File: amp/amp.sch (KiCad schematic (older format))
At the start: 29 parts

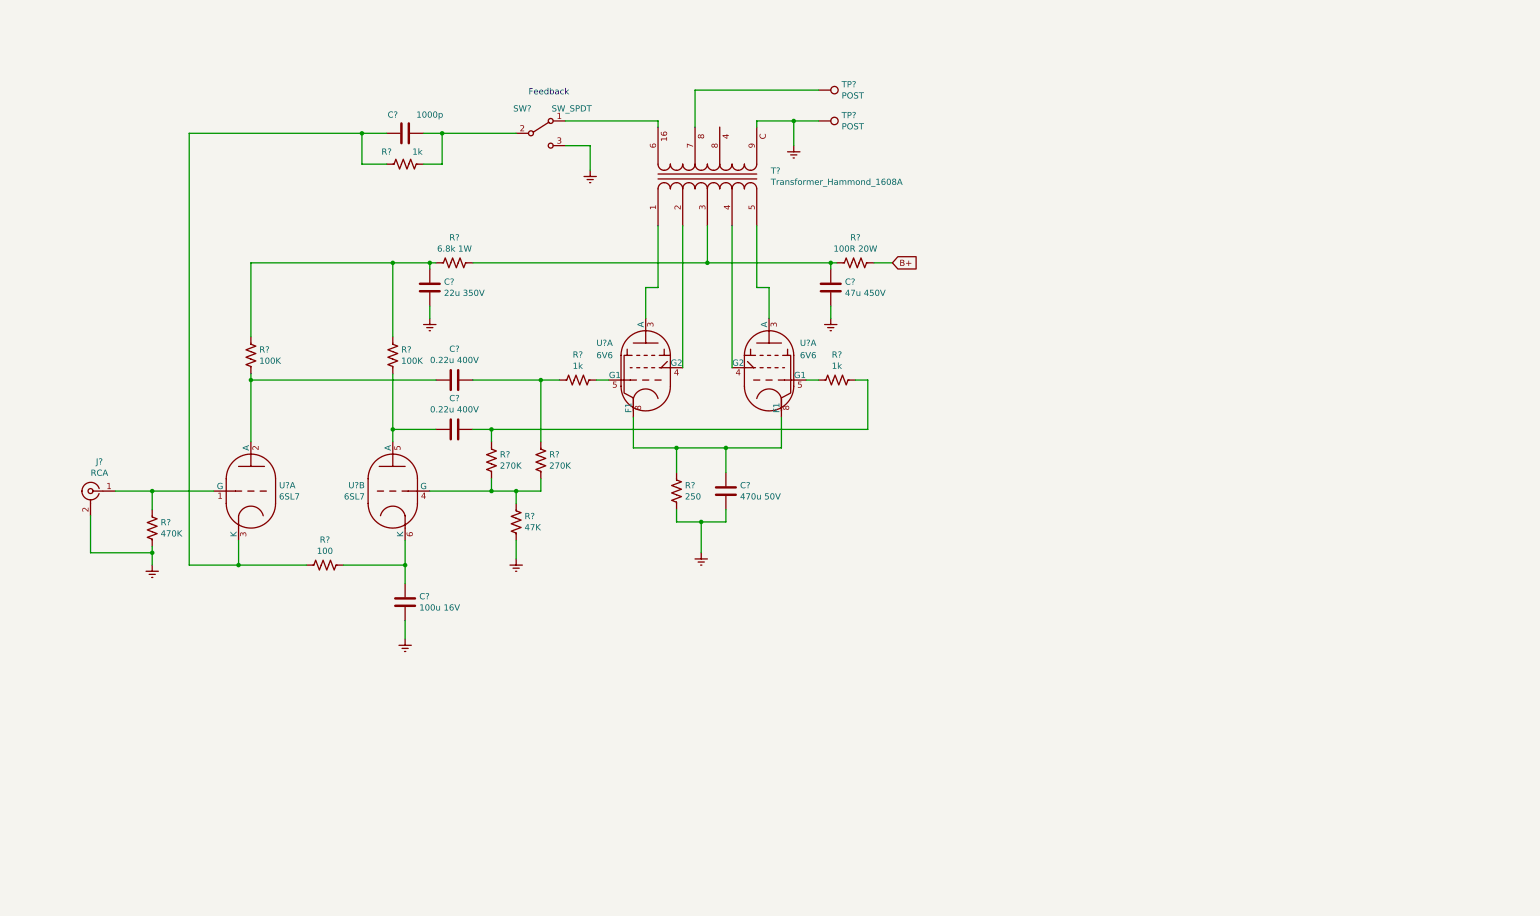
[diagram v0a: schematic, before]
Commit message: draft stereo schem complete
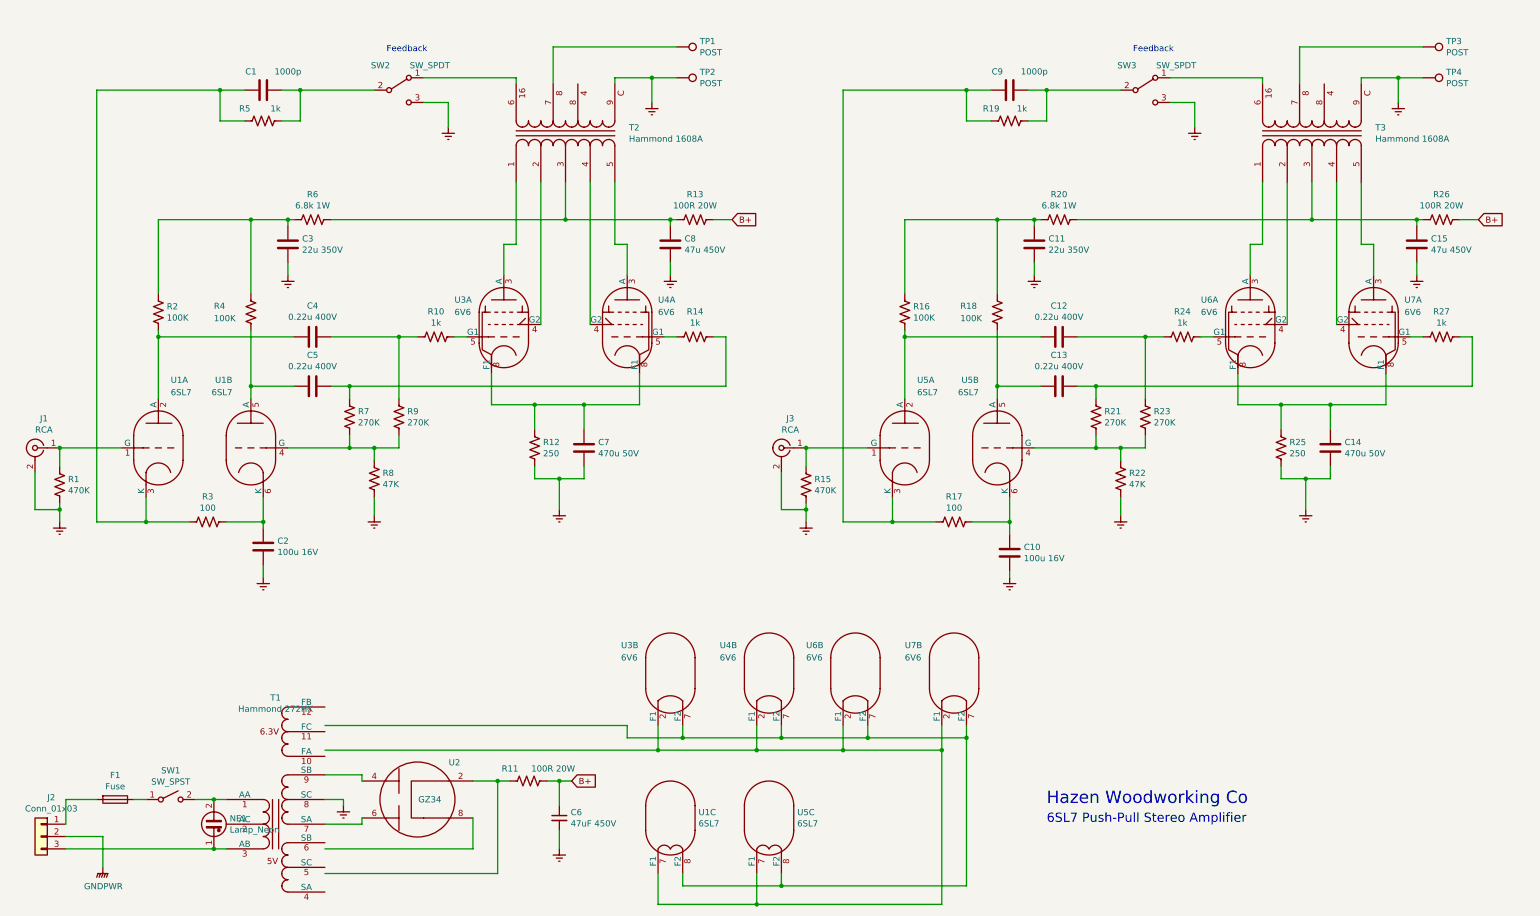
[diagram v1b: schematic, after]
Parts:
- added C10: 100u 16V, symbol Device:C
- added C11: 22u 350V, symbol Device:C
- added C12, C13: 0.22u 400V, symbol Device:C
- added C14: 470u 50V, symbol Device:C
- added C15: 47u 450V, symbol Device:C
- added C6: 47uF 450V, symbol Device:C_Small
- added C9: 1000p, symbol Device:C
- added F1: Fuse, symbol Device:Fuse
- added J2: Conn_01x03, symbol Connector_Generic:Conn_01x03
- added J3: RCA, symbol Connector:Conn_Coaxial
- added NE1: Lamp_Neon, symbol Device:Lamp_Neon
- added R11, R26: 100R 20W, symbol Device:R_US
- added R15: 470K, symbol Device:R_US
- added R16, R18: 100K, symbol Device:R_US
- added R17: 100, symbol Device:R_US
- added R19, R24, R27: 1k, symbol Device:R_US
- added R20: 6.8k 1W, symbol Device:R_US
- added R21, R23: 270K, symbol Device:R_US
- added R22: 47K, symbol Device:R_US
- added R25: 250, symbol Device:R_US
- added SW1: SW_SPST, symbol Switch:SW_SPST
- added SW3: SW_SPDT, symbol Switch:SW_SPDT
- added T1: Hammond 272HX, symbol my_tubes:Transformer_tube_power_dualfil
- added T3: Hammond 1608A, symbol my_tubes:Transformer_Hammond_1608A
- added TP3, TP4: POST, symbol Connector:TestPoint
- added unit 3 of U1
- added U2: GZ34, symbol my_tubes:GZ34
- added unit 2 of U3
- added unit 2 of U4
- added U5: 6SL7, Valve:Valve_Noval_P, symbol my_tubes:6SL7
- added U6, U7: 6V6, Valve:Valve_Octal, symbol my_tubes:6V6
- T2: renamed from T?; value Transformer_Hammond_1608A -> Hammond 1608A
- gave numbers to parts that had none: 27
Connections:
- net B+: now also C6.1, R11.1, R26.1
- net Earth: now also C10.1, C11.1, C14.1, C15.1, C6.2, J3.2 (Ext), R15.2, R22.2, R25.2, SW3.3 (C), T1.8 (SC), T3.9 (BLK), TP4.1
- new net: NE1.2, SW1.2 (B), T1.1 (AA)
- new net: J2.3 (Pin_3), NE1.1, T1.3 (AB)
- new net: T1.7 (SA), U2.6 (A2)
- new net: T1.9 (SB), U2.4 (A1)
- new net: R11.2, U2.2 (K)
- new net: U1.7 (F1), U3.2 (F1), U4.2 (F1), U5.7 (F1), U6.2 (F1), U7.2 (F1)
- new net: U1.8 (F2), U3.7 (F2), U4.7 (F2), U5.8 (F2), U6.7 (F2), U7.7 (F2)
- new net: T3.1 (BLU), U6.3 (A)
- new net: T3.2 (BLU/YEL), U6.4 (G2)
- new net: R24.1, U6.5 (G1)
- new net: C14.2, R25.1, U6.8 (F1), U7.8 (F1)
- new net: J3.1 (In), R15.1, U5.1 (G)
- new net: C12.2, R16.2, U5.2 (A)
- new net: C9.2, R17.2, R19.2, U5.3 (K)
- new net: R21.2, R22.1, R23.2, U5.4 (G)
- new net: C13.2, R18.2, U5.5 (A)
- new net: C10.2, R17.1, U5.6 (K)
- new net: C11.2, R16.1, R18.1, R20.2
- new net: T3.5 (BRN), U7.3 (A)
- new net: T3.4 (BRN/YEL), U7.4 (G2)
- new net: R27.2, U7.5 (G1)
- new net: C12.1, R23.1, R24.2
- new net: C13.1, R21.1, R27.1
- new net: C15.2, R20.1, R26.2, T3.3 (RED)
- new net: SW3.1 (A), T3.6 (WHT)
- new net: T3.7 (YEL), TP3.1
- new net: C9.1, R19.1, SW3.2 (B)
- new net: F1.1, SW1.1 (A)
- new net: F1.2, J2.1 (Pin_1)
- new net GNDPWR: J2.2 (Pin_2)
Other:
- note added: "6SL7 Push-Pull Stereo Amplifier"
- note added: "Hazen Woodworking Co"
- moved on the sheet: C1, C2, C3, C4, C5, C7, C8, J1, R1, R10, R12, R13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

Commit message: starting footprints
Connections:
- net Earth: now also T1.11 (FC)
- net at T1.10 (FA): now also U1.7 (F1), U3.2 (F1), U4.2 (F1), U5.7 (F1), U6.2 (F1), U7.2 (F1)
- net at T1.12 (FB): now also U1.8 (F2), U3.7 (F2), U4.7 (F2), U5.8 (F2), U6.7 (F2), U7.7 (F2)
- net at T1.4 (SA): now also R11.2, U2.2 (K)
- net at T1.6 (SB): now also U2.8 (F2)
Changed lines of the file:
@@
 U 1 1 629E47F8
 P 2650 6900
-F 0 "T1" H 2650 7725 50  0000 C CNN
-F 1 "Hammond 272HX" H 2650 7634 50  0000 C CNN
+F 0 "T1" H 2500 7900 50  0000 C CNN
+F 1 "Hammond 272HX" H 2800 7800 50  0000 C CNN
 F 2 "" H 2650 6700 50  0001 C CNN
 F 3 "~" H 2650 6700 50  0001 C CNN
@@
 	3200 6900 3050 6900
 Wire Wire Line
-	3050 7300 4250 7300
-Wire Wire Line
-	4250 7300 4250 7050
-Wire Wire Line
-	3050 7500 4450 7500
-Wire Wire Line
-	4450 7500 4450 6750
+	3050 7250 4250 7250
+Wire Wire Line
+	4250 7250 4250 7050
+Wire Wire Line
+	3050 7650 4450 7650
+Wire Wire Line
+	4450 7650 4450 6750
 Wire Wire Line
 	4450 6750 4250 6750
@@
 Connection ~ 8250 6400
 Wire Wire Line
-	5750 6500 3050 6500
-Connection ~ 5750 6500
-Wire Wire Line
-	3050 6300 5500 6300
-Wire Wire Line
-	5500 6300 5500 6400
+	3050 6150 5500 6150
+Wire Wire Line
+	5500 6150 5500 6400
 Wire Wire Line
 	5500 6400 5950 6400
@@
 U 1 1 62BAE772
 P 2150 7100
-F 0 "NE1" H 2278 7146 50  0000 L CNN
-F 1 "Lamp_Neon" H 2278 7055 50  0000 L CNN
+F 0 "NE1" H 1850 7100 50  0000 L CNN
+F 1 "Lamp_Neon" H 1850 6800 50  0000 L CNN
 F 2 "" V 2150 7200 50  0001 C CNN
 F 3 "~" V 2150 7200 50  0001 C CNN
@@
 Text Notes 8900 6950 0    100  ~ 0
 Hazen Woodworking Co
+Wire Wire Line
+	3050 6550 5500 6550
+Wire Wire Line
+	5500 6550 5500 6500
+Wire Wire Line
+	5500 6500 5750 6500
+Connection ~ 5750 6500
+$Comp
+L power:Earth #PWR?
+U 1 1 62A64B63
+P 3200 6350
+F 0 "#PWR?" H 3200 6100 50  0001 C CNN
+F 1 "Earth" H 3200 6200 50  0001 C CNN
+F 2 "" H 3200 6350 50  0001 C CNN
+F 3 "~" H 3200 6350 50  0001 C CNN
+	1    3200 6350
+	1    0    0    -1
+$EndComp
+Wire Wire Line
+	3200 6350 3050 6350
 $EndSCHEMATC

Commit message: working on schem
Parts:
- removed J2: Conn_01x03, symbol Connector_Generic:Conn_01x03
- removed T1: Hammond 272HX, symbol my_tubes:Transformer_tube_power_dualfil
- added J?: Conn_01x05, symbol Connector_Generic:Conn_01x05
- added JP?: JPR3, symbol Device:Jumper_NC_Dual
- added R?: RRRRR, symbol Device:R_US
- added T?: Transformer_Hammond_272HX, symbol my_tubes:Transformer_Hammond_272HX
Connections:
- net Earth: now also T?.11 (FC), T?.8 (SC)
- net GNDPWR: now also J?.2 (Pin_2), J?.4 (Pin_4), J?.5 (Pin_5)
- net at SW1.2 (B): now also JP?.2, R?.2; no longer NE1.2
- net at U1.7 (F1), U3.2 (F1), U4.2 (F1)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: now also T?.10 (FA)
- net at U1.8 (F2), U3.7 (F2), U4.7 (F2)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: now also T?.12 (FB)
- net at NE1.1: now also J?.3 (Pin_3), T?.3 (AB)
- net at R11.2, U2.2 (K): now also T?.4 (SA)
- net at U2.8 (F2): now also T?.6 (SB)
- net at U2.6 (A2): now also T?.7 (SA)
- net at U2.4 (A1): now also T?.9 (SB)
- net at F1.2: now also J?.1 (Pin_1)
- new net: JP?.1, T?.1 (AA)
- new net: JP?.3, T?.2 (AC)
- new net: NE1.2, R?.1
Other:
- note added: "117V"
- note added: "125V"
- moved on the sheet: F1, NE1, SW1
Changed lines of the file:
@@
 Feedback
-$Comp
-L my_tubes:Transformer_tube_power_dualfil T1
-U 1 1 629E47F8
-P 2650 6900
-F 0 "T1" H 2500 7900 50  0000 C CNN
-F 1 "Hammond 272HX" H 2800 7800 50  0000 C CNN
-F 2 "" H 2650 6700 50  0001 C CNN
-F 3 "~" H 2650 6700 50  0001 C CNN
-	1    2650 6900
-	1    0    0    -1
-$EndComp
 $Comp
 L my_tubes:GZ34 U2
@@
 L Device:Fuse F1
 U 1 1 62BAA6BB
-P 1350 6900
-F 0 "F1" V 1153 6900 50  0000 C CNN
-F 1 "Fuse" V 1244 6900 50  0000 C CNN
-F 2 "" V 1280 6900 50  0001 C CNN
-F 3 "~" H 1350 6900 50  0001 C CNN
-	1    1350 6900
+P 1300 5950
+F 0 "F1" V 1103 5950 50  0000 C CNN
+F 1 "Fuse" V 1194 5950 50  0000 C CNN
+F 2 "" V 1230 5950 50  0001 C CNN
+F 3 "~" H 1300 5950 50  0001 C CNN
+	1    1300 5950
 	0    1    1    0
 $EndComp
@@
 L Switch:SW_SPST SW1
 U 1 1 62BACA0A
-P 1800 6900
-F 0 "SW1" H 1800 7135 50  0000 C CNN
-F 1 "SW_SPST" H 1800 7044 50  0000 C CNN
-F 2 "" H 1800 6900 50  0001 C CNN
-F 3 "~" H 1800 6900 50  0001 C CNN
-	1    1800 6900
+P 1700 5950
+F 0 "SW1" H 1700 6185 50  0000 C CNN
+F 1 "SW_SPST" H 1700 6094 50  0000 C CNN
+F 2 "" H 1700 5950 50  0001 C CNN
+F 3 "~" H 1700 5950 50  0001 C CNN
+	1    1700 5950
 	1    0    0    -1
 $EndComp
@@
 L Device:Lamp_Neon NE1
 U 1 1 62BAE772
-P 2150 7100
-F 0 "NE1" H 1850 7100 50  0000 L CNN
-F 1 "Lamp_Neon" H 1850 6800 50  0000 L CNN
-F 2 "" V 2150 7200 50  0001 C CNN
-F 3 "~" V 2150 7200 50  0001 C CNN
-	1    2150 7100
-	1    0    0    -1
-$EndComp
-Wire Wire Line
-	2000 6900 2150 6900
-Wire Wire Line
-	2150 6900 2250 6900
-Connection ~ 2150 6900
-Wire Wire Line
-	2150 7300 2250 7300
-Connection ~ 2150 7300
-Wire Wire Line
-	1500 6900 1600 6900
-$Comp
-L Connector_Generic:Conn_01x03 J2
-U 1 1 62BFDA53
-P 750 7200
-F 0 "J2" H 668 7517 50  0000 C CNN
-F 1 "Conn_01x03" H 668 7426 50  0000 C CNN
-F 2 "" H 750 7200 50  0001 C CNN
-F 3 "~" H 750 7200 50  0001 C CNN
-	1    750  7200
-	-1   0    0    -1
-$EndComp
-Wire Wire Line
-	950  7300 2150 7300
-Wire Wire Line
-	950  7100 950  6900
-Wire Wire Line
-	950  6900 1200 6900
-Wire Wire Line
-	950  7200 1250 7200
-Wire Wire Line
-	1250 7200 1250 7450
+P 1400 7100
+F 0 "NE1" H 1100 7100 50  0000 L CNN
+F 1 "Lamp_Neon" H 1100 6800 50  0000 L CNN
+F 2 "" V 1400 7200 50  0001 C CNN
+F 3 "~" V 1400 7200 50  0001 C CNN
+	1    1400 7100
+	1    0    0    -1
+$EndComp
+Wire Wire Line
+	1400 7300 2250 7300
+Connection ~ 1400 7300
+Wire Wire Line
+	1450 5950 1500 5950
+Wire Wire Line
+	1200 6050 1200 6250
 $Comp
 L power:GNDPWR #PWR02
 U 1 1 62C28C1D
-P 1250 7450
-F 0 "#PWR02" H 1250 7250 50  0001 C CNN
-F 1 "GNDPWR" H 1254 7296 50  0000 C CNN
-F 2 "" H 1250 7400 50  0001 C CNN
-F 3 "" H 1250 7400 50  0001 C CNN
-	1    1250 7450
+P 1200 6550
+F 0 "#PWR02" H 1200 6350 50  0001 C CNN
+F 1 "GNDPWR" H 1204 6396 50  0000 C CNN
+F 2 "" H 1200 6500 50  0001 C CNN
+F 3 "" H 1200 6500 50  0001 C CNN
+	1    1200 6550
 	1    0    0    -1
 $EndComp
@@
 Wire Wire Line
 	3200 6350 3050 6350
+$Comp
+L my_tubes:Transformer_Hammond_272HX T?
+U 1 1 62A17279
+P 2650 6900
+F 0 "T?" H 2800 7900 50  0000 C CNN
+F 1 "Transformer_Hammond_272HX" H 3350 7800 50  0000 C CNN
+F 2 "" H 2650 6700 50  0001 C CNN
+F 3 "~" H 2650 6700 50  0001 C CNN
+	1    2650 6900
+	1    0    0    -1
+$EndComp
+$Comp
+L Connector_Generic:Conn_01x05 J?
+U 1 1 62A2A230
+P 700 6150
+F 0 "J?" H 618 6567 50  0000 C CNN
+F 1 "Conn_01x05" H 618 6476 50  0000 C CNN
+F 2 "" H 700 6150 50  0001 C CNN
+F 3 "~" H 700 6150 50  0001 C CNN
+	1    700  6150
+	-1   0    0    -1
+$EndComp
+Wire Wire Line
+	1150 5950 900  5950
+Wire Wire Line
+	900  6250 1200 6250
+Connection ~ 1200 6250
+Wire Wire Line
+	1200 6250 1200 6350
+Wire Wire Line
+	900  6350 1200 6350
+Connection ~ 1200 6350
+Wire Wire Line
+	1200 6350 1200 6550
+Wire Wire Line
+	1200 6050 900  6050
+Wire Wire Line
+	900  6150 1000 6150
+Wire Wire Line
+	1000 6150 1000 7300
+Wire Wire Line
+	1000 7300 1400 7300
+$Comp
+L Device:Jumper_NC_Dual JP?
+U 1 1 62B13A04
+P 2000 6400
+F 0 "JP?" H 2000 6547 50  0000 C CNN
+F 1 "JPR3" H 2000 6638 50  0000 C CNN
+F 2 "" H 2000 6400 50  0001 C CNN
+F 3 "~" H 2000 6400 50  0001 C CNN
+	1    2000 6400
+	-1   0    0    1
+$EndComp
+Wire Wire Line
+	1900 5950 2000 5950
+Wire Wire Line
+	2000 5950 2000 6150
+Wire Wire Line
+	2250 6400 2250 6900
+Wire Wire Line
+	1750 7100 1750 6400
+Wire Wire Line
+	1750 7100 2250 7100
+$Comp
+L Device:R_US R?
+U 1 1 62B96FFD
+P 1400 6450
+F 0 "R?" V 1300 6300 50  0000 C CNN
+F 1 "RRRRR" V 1300 6650 50  0000 C CNN
+F 2 "" V 1440 6440 50  0001 C CNN
+F 3 "~" H 1400 6450 50  0001 C CNN
+	1    1400 6450
+	-1   0    0    1
+$EndComp
+Wire Wire Line
+	1400 6300 1400 6150
+Wire Wire Line
+	1400 6150 2000 6150
+Connection ~ 2000 6150
+Wire Wire Line
+	2000 6150 2000 6300
+Wire Wire Line
+	1400 6600 1400 6900
+Text Notes 2050 6300 0    50   ~ 0
+125V
+Text Notes 1750 6300 0    50   ~ 0
+117V
 $EndSCHEMATC

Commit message: working on schem
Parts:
- removed SW1: SW_SPST, symbol Switch:SW_SPST
- added J? (x2): JPR_2x3, symbol Connector_Generic:Conn_02x03_Odd_Even
- added SW?: SW_SPST_GND, symbol my_tubes:SW_SPST_GND
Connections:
- net Earth: now also SW?.4 (G1), SW?.5 (G2)
- net at SW2.1 (A), T2.6 (WHT): now also J?.1 (Pin_1)
- net at T2.7 (YEL): now also J?.3 (Pin_3); no longer TP1.1
- net at T2.8 (GRN): now also J?.5 (Pin_5)
- net at SW3.1 (A), T3.6 (WHT): now also J?.1 (Pin_1)
- net at T3.7 (YEL): now also J?.3 (Pin_3); no longer TP3.1
- net at T3.8 (GRN): now also J?.5 (Pin_5)
- net at JP?.2, R?.2: now also SW?.2 (B)
- net at F1.1: now also SW?.1 (A)
- new net: J?.2 (Pin_2), J?.4 (Pin_4), J?.6 (Pin_6), TP1.1
- new net: J?.2 (Pin_2), J?.4 (Pin_4), J?.6 (Pin_6), TP3.1
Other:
- moved on the sheet: JP?
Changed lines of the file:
@@
 $EndComp
-Wire Wire Line
-	4900 1100 4900 800
-Wire Wire Line
-	4900 800  5900 800
 Wire Wire Line
 	5700 1050 5900 1050
@@
 $EndComp
 Wire Wire Line
-	10950 1100 10950 800
-Wire Wire Line
-	10950 800  11950 800
-Wire Wire Line
 	11750 1050 11950 1050
 Connection ~ 11750 1050
@@
 $EndComp
 $Comp
-L Switch:SW_SPST SW1
-U 1 1 62BACA0A
-P 1700 5950
-F 0 "SW1" H 1700 6185 50  0000 C CNN
-F 1 "SW_SPST" H 1700 6094 50  0000 C CNN
-F 2 "" H 1700 5950 50  0001 C CNN
-F 3 "~" H 1700 5950 50  0001 C CNN
-	1    1700 5950
-	1    0    0    -1
-$EndComp
-$Comp
 L Device:Lamp_Neon NE1
 U 1 1 62BAE772
@@
 L Device:Jumper_NC_Dual JP?
 U 1 1 62B13A04
-P 2000 6400
-F 0 "JP?" H 2000 6547 50  0000 C CNN
-F 1 "JPR3" H 2000 6638 50  0000 C CNN
-F 2 "" H 2000 6400 50  0001 C CNN
-F 3 "~" H 2000 6400 50  0001 C CNN
-	1    2000 6400
+P 2000 6550
+F 0 "JP?" H 2000 6697 50  0000 C CNN
+F 1 "JPR3" H 2000 6788 50  0000 C CNN
+F 2 "" H 2000 6550 50  0001 C CNN
+F 3 "~" H 2000 6550 50  0001 C CNN
+	1    2000 6550
 	-1   0    0    1
 $EndComp
@@
 	1900 5950 2000 5950
 Wire Wire Line
-	2000 5950 2000 6150
-Wire Wire Line
-	2250 6400 2250 6900
-Wire Wire Line
-	1750 7100 1750 6400
+	2000 5950 2000 6200
+Wire Wire Line
+	2250 6550 2250 6900
+Wire Wire Line
+	1750 7100 1750 6550
 Wire Wire Line
 	1750 7100 2250 7100
@@
 $EndComp
 Wire Wire Line
-	1400 6300 1400 6150
-Wire Wire Line
-	1400 6150 2000 6150
-Connection ~ 2000 6150
-Wire Wire Line
-	2000 6150 2000 6300
+	1400 6300 1400 6200
+Wire Wire Line
+	1400 6200 2000 6200
+Connection ~ 2000 6200
+Wire Wire Line
+	2000 6200 2000 6450
 Wire Wire Line
 	1400 6600 1400 6900
@@
 Text Notes 1750 6300 0    50   ~ 0
 117V
+$Comp
+L Connector_Generic:Conn_02x03_Odd_Even J?
+U 1 1 62A3351D
+P 5450 800
+F 0 "J?" H 5150 1050 50  0000 C CNN
+F 1 "JPR_2x3" H 5500 1026 50  0000 C CNN
+F 2 "" H 5450 800 50  0001 C CNN
+F 3 "~" H 5450 800 50  0001 C CNN
+	1    5450 800
+	1    0    0    -1
+$EndComp
+Wire Wire Line
+	5750 700  5750 800
+Wire Wire Line
+	5750 800  5750 900
+Connection ~ 5750 800
+Wire Wire Line
+	5750 800  5900 800
+Wire Wire Line
+	5250 700  4600 700
+Wire Wire Line
+	4600 700  4600 1050
+Connection ~ 4600 1050
+Wire Wire Line
+	5250 800  4900 800
+Wire Wire Line
+	4900 800  4900 1100
+Wire Wire Line
+	5250 900  5100 900
+Wire Wire Line
+	5100 900  5100 1100
+$Comp
+L Connector_Generic:Conn_02x03_Odd_Even J?
+U 1 1 62A982B1
+P 11500 800
+F 0 "J?" H 11250 1050 50  0000 C CNN
+F 1 "JPR_2x3" H 11550 1026 50  0000 C CNN
+F 2 "" H 11500 800 50  0001 C CNN
+F 3 "~" H 11500 800 50  0001 C CNN
+	1    11500 800
+	1    0    0    -1
+$EndComp
+Wire Wire Line
+	11800 700  11800 800
+Wire Wire Line
+	11800 800  11800 900
+Connection ~ 11800 800
+Wire Wire Line
+	11800 800  11950 800
+Wire Wire Line
+	11300 700  10650 700
+Wire Wire Line
+	10650 700  10650 1050
+Wire Wire Line
+	11300 800  10950 800
+Wire Wire Line
+	10950 800  10950 1100
+Wire Wire Line
+	11300 900  11150 900
+Wire Wire Line
+	11150 900  11150 1100
+Connection ~ 10650 1050
+$Comp
+L my_tubes:SW_SPST_GND SW?
+U 1 1 62ABDF9D
+P 1700 5950
+F 0 "SW?" H 1700 6185 50  0000 C CNN
+F 1 "SW_SPST_GND" H 1700 6094 50  0000 C CNN
+F 2 "" H 1700 5950 50  0001 C CNN
+F 3 "~" H 1700 5950 50  0001 C CNN
+	1    1700 5950
+	1    0    0    -1
+$EndComp
+Wire Wire Line
+	1650 6100 1750 6100
+Wire Wire Line
+	1750 6100 2350 6100
+Connection ~ 1750 6100
+$Comp
+L power:Earth #PWR?
+U 1 1 62AE30E6
+P 2350 6100
+F 0 "#PWR?" H 2350 5850 50  0001 C CNN
+F 1 "Earth" H 2350 5950 50  0001 C CNN
+F 2 "" H 2350 6100 50  0001 C CNN
+F 3 "~" H 2350 6100 50  0001 C CNN
+	1    2350 6100
+	1    0    0    -1
+$EndComp
 $EndSCHEMATC

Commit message: working on schem
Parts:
- J?: footprint (none) -> GSP1_power_entry:GSP1.8101.1
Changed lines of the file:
@@
 F 0 "J?" H 618 6567 50  0000 C CNN
 F 1 "Conn_01x05" H 618 6476 50  0000 C CNN
-F 2 "" H 700 6150 50  0001 C CNN
+F 2 "GSP1_power_entry:GSP1.8101.1" H 700 6150 50  0001 C CNN
 F 3 "~" H 700 6150 50  0001 C CNN
 	1    700  6150
